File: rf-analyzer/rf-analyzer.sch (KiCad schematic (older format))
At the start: 56 parts, among them U1 AD8302, U2 AD8302, U3 OPA695

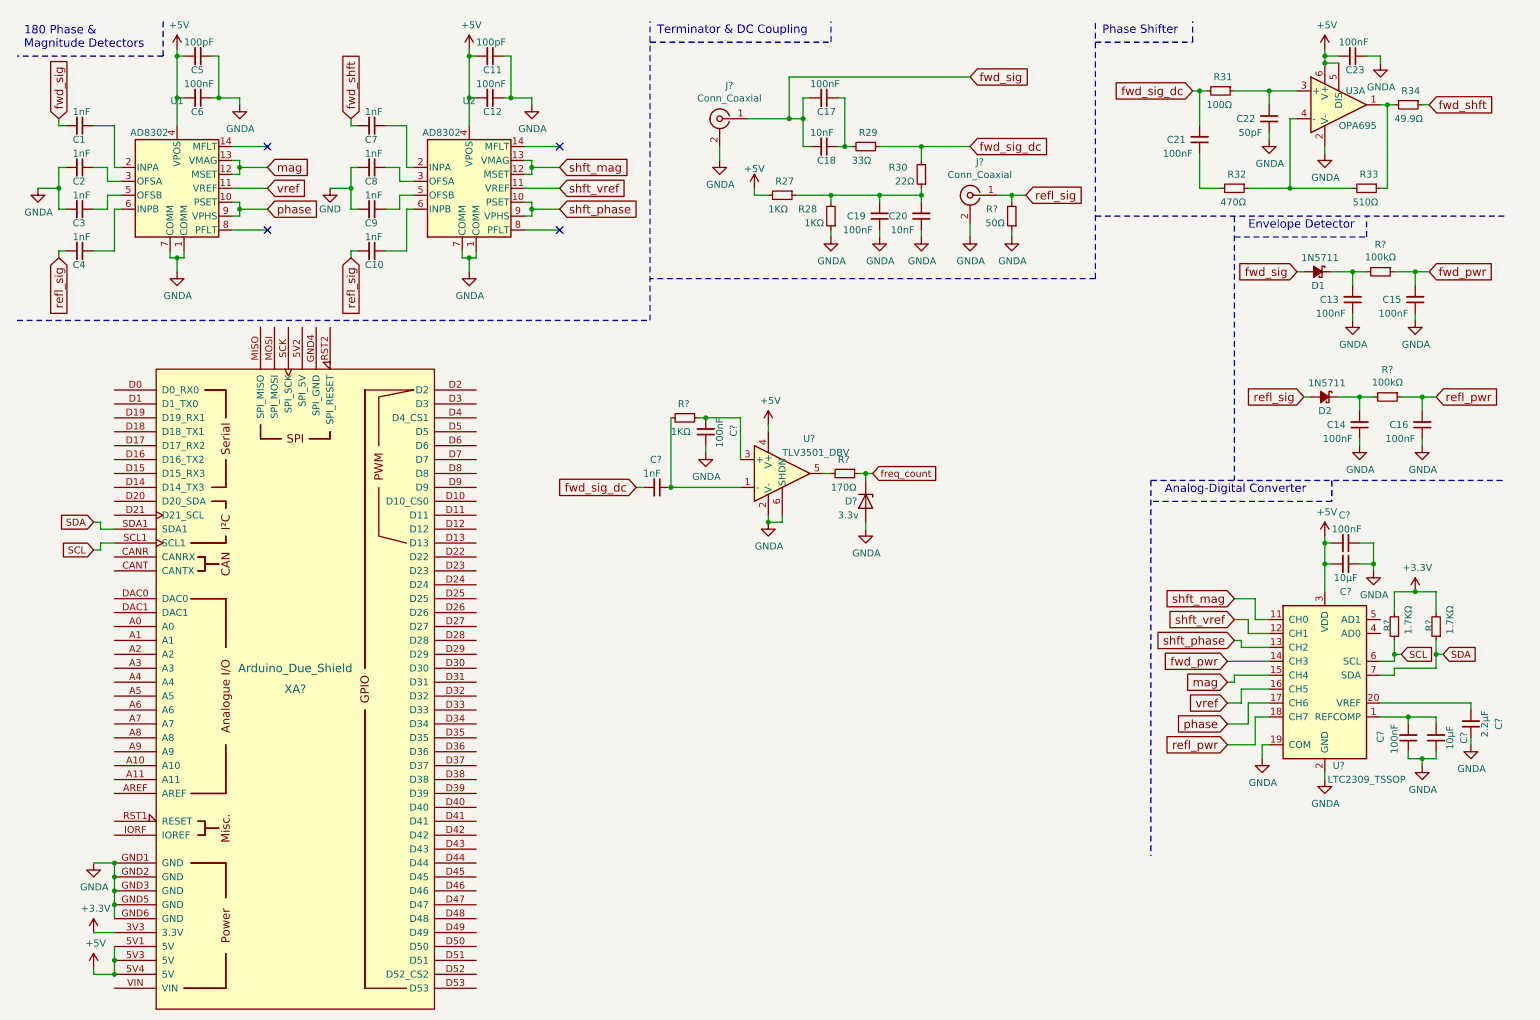
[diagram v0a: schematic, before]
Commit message: Added frequency counter prescaler.
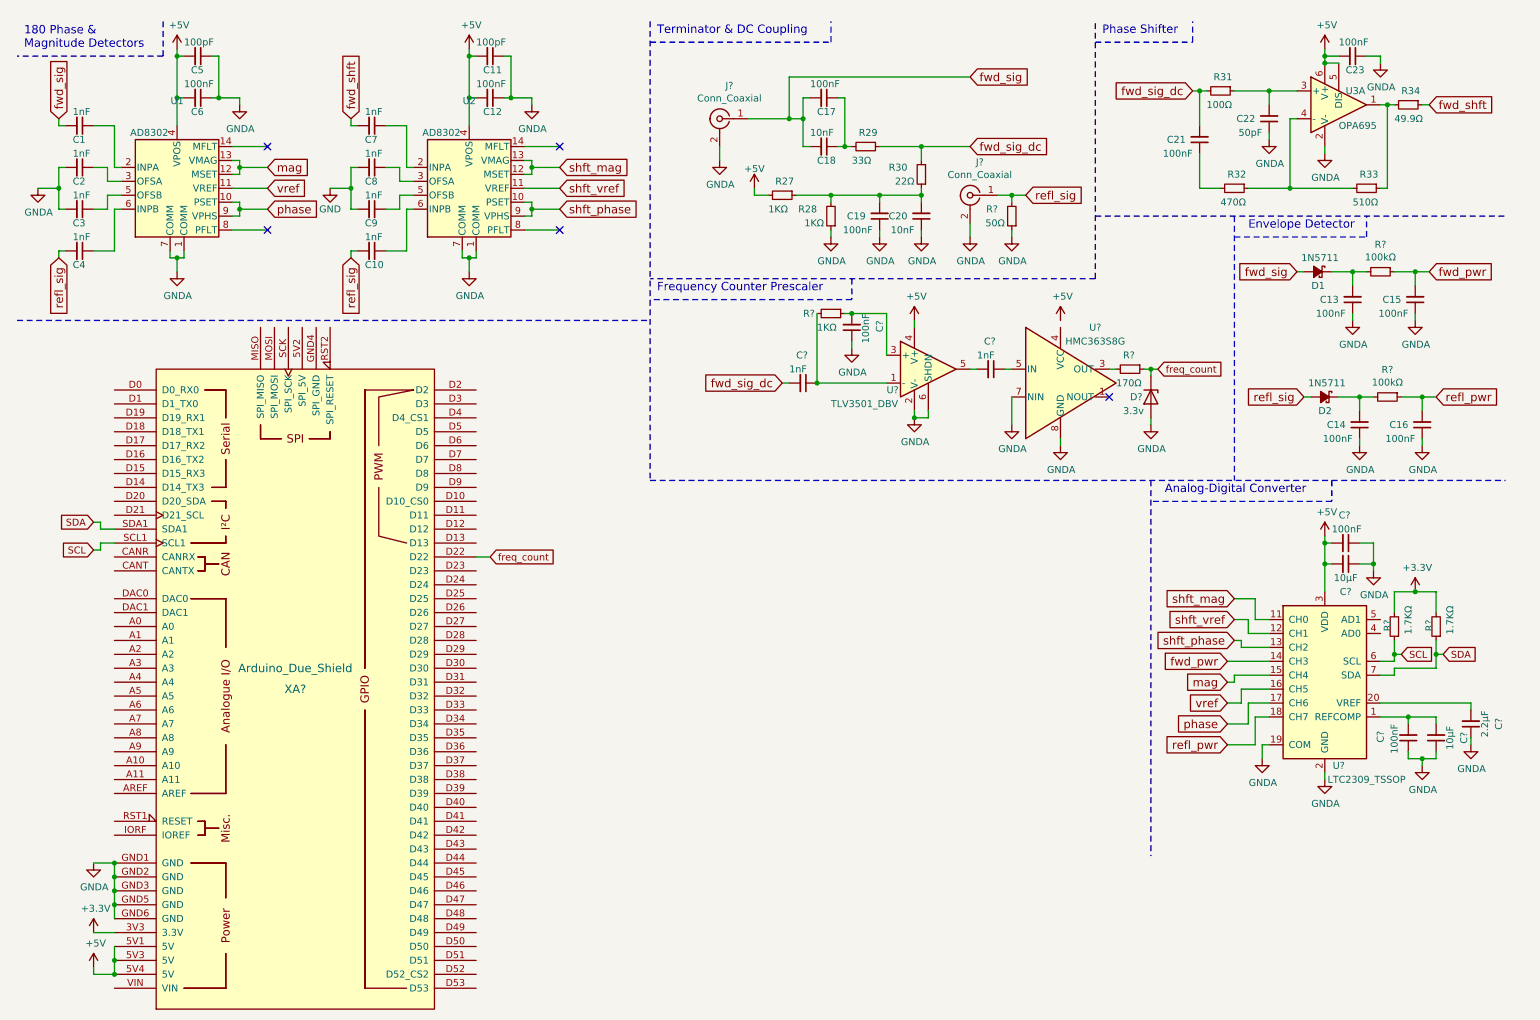
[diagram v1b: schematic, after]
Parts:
- added C?: 1nF, Capacitor_SMD:C_0603_1608Metric_Pad1.05x0.95mm_HandSolder, symbol Device:C_Small
- added U?: HMC363S8G, Package_SO:SOIC-8_3.9x4.9mm_P1.27mm, symbol RF_Freemo:HMC363S8G
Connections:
- net GNDA: now also U?.7 (NIN), U?.8 (GND)
- net freq_count: now also XA?.D22
- net at R?.2: now also U?.3 (OUT); no longer U?.5
- new net: C?.1, U?.5 (IN)
- new net: C?.2, U?.5
- no-connect marks 4 -> 5
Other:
- note added: "Frequency Counter Prescaler"
- moved on the sheet: C?, D?, R?, U?

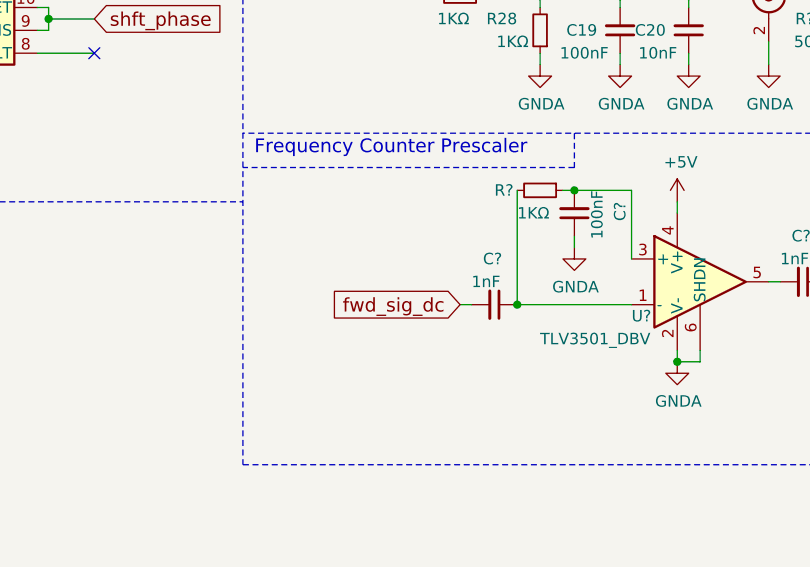
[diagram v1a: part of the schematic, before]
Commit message: Removed decoupling capacitor from prescaler.
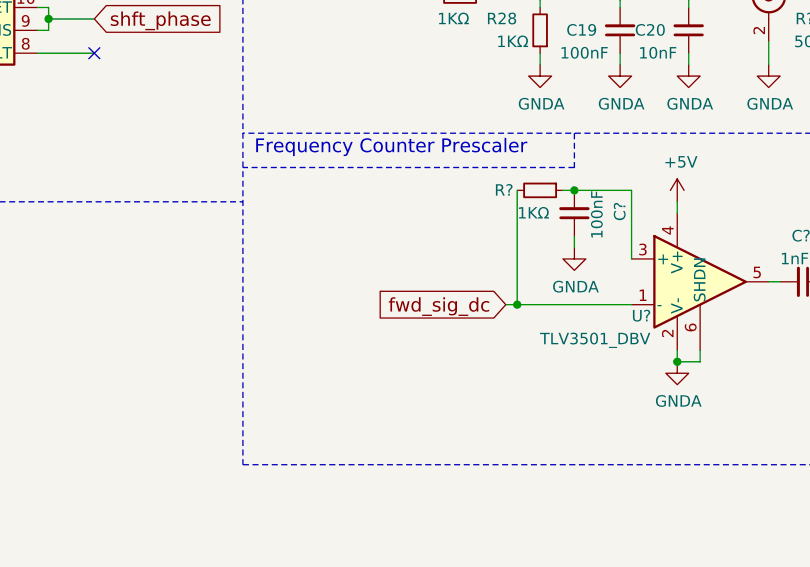
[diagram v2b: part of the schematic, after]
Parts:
- removed C?: 1nF, Capacitor_SMD:C_0603_1608Metric_Pad1.05x0.95mm_HandSolder, symbol Device:C_Small
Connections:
- net fwd_sig_dc: now also R?.2, U?.1 (-)
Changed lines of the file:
@@
 Connection ~ 9900 800
-$Comp
-L Device:C_Small C?
-U 1 1 604F0B98
-P 6150 3100
-F 0 "C?" V 5950 3050 50  0000 L CNN
-F 1 "1nF" V 6050 3000 50  0000 L CNN
-F 2 "Capacitor_SMD:C_0603_1608Metric_Pad1.05x0.95mm_HandSolder" H 6150 3100 50  0001 C CNN
-F 3 "" H 6150 3100 50  0001 C CNN
-	1    6150 3100
-	0    1    1    0
-$EndComp
 $Comp
 L power:GNDA #PWR?
@@
 Wire Wire Line
 	6250 3100 6750 3100
-Connection ~ 6250 3100
 $Comp
 L power:GNDA #PWR?
@@
 	7050 3350 6950 3350
 Connection ~ 6950 3350
-Text GLabel 6000 3100 0    60   Input ~ 0
+Text GLabel 6200 3100 0    60   Input ~ 0
 fwd_sig_dc
 Wire Wire Line
-	6000 3100 6050 3100
+	6200 3100 6250 3100
 $Comp
 L Device:R_Small R?
@@
 	1    0    0    -1
 $EndComp
+Connection ~ 6250 3100
 $EndSCHEMATC

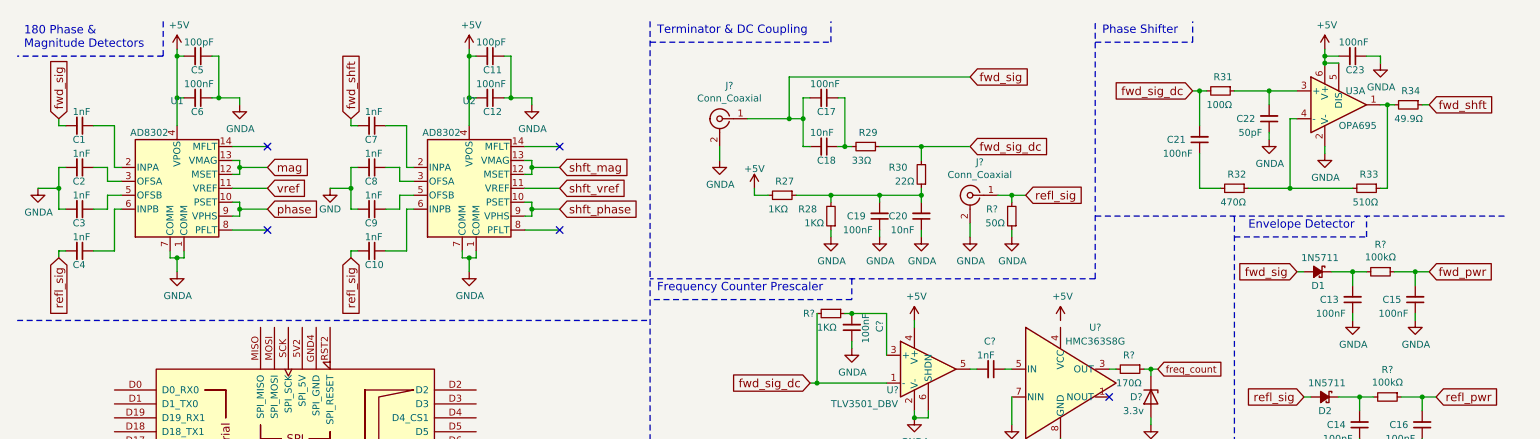
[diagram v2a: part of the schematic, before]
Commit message: Added the decoupling caps in a central location allowing me to reduce the overall number of capacitors.
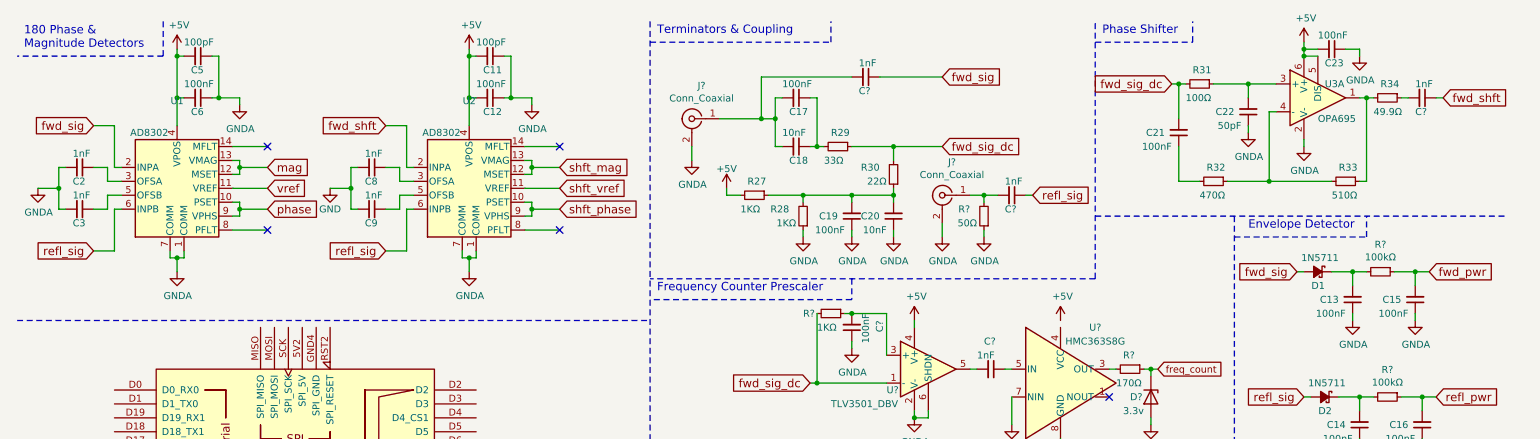
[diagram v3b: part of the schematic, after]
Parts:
- removed C1, C10, C4, C7: 1nF, Capacitor_SMD:C_0603_1608Metric_Pad1.05x0.95mm_HandSolder, symbol Device:C_Small
- added C? (x3): 1nF, Capacitor_SMD:C_0603_1608Metric_Pad1.05x0.95mm_HandSolder, symbol Device:C_Small
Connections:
- net fwd_shft: now also U2.2 (INPA), C?.1; no longer R34.1
- net fwd_sig: now also U1.2 (INPA), C?.1; no longer C17.2, C18.2, J?.1 (In)
- net refl_sig: now also U1.6 (INPB), U2.6 (INPB), C?.1; no longer J?.1 (In), R?.2
- new net: C?.2, R34.1
- new net: C17.2, C18.2, C?.2, J?.1 (In)
- new net: C?.2, J?.1 (In), R?.2
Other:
- note added: "Terminators & Coupling"
- note removed: "Terminator & DC Coupling"
- moved on the sheet: C17, C18, C19, C20, C21, C22, C23, J?, R27, R28, R29, R30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

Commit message: Added shielding to schematic.
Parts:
- added J?: RF_Shield_Two_Pieces, RF_Shielding:Laird_Technologies_BMI-S-230-F_50.8x38.1mm, symbol Device:RF_Shield_Two_Pieces
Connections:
- net GNDA: now also J?.1 (Shield)
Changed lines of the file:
@@
 Wire Wire Line
 	10750 1050 10700 1050
+$Comp
+L Device:RF_Shield_Two_Pieces J?
+U 1 1 5FB2E8F5
+P 5750 4800
+F 0 "J?" H 6480 4864 50  0000 L CNN
+F 1 "RF_Shield_Two_Pieces" H 6480 4773 50  0000 L CNN
+F 2 "RF_Shielding:Laird_Technologies_BMI-S-230-F_50.8x38.1mm" H 5750 4700 50  0001 C CNN
+F 3 "~" H 5750 4700 50  0001 C CNN
+	1    5750 4800
+	1    0    0    -1
+$EndComp
+$Comp
+L power:GNDA #PWR?
+U 1 1 5FB3AD55
+P 5750 5250
+F 0 "#PWR?" H 5750 5000 50  0001 C CNN
+F 1 "GNDA" H 5755 5077 50  0000 C CNN
+F 2 "" H 5750 5250 50  0001 C CNN
+F 3 "" H 5750 5250 50  0001 C CNN
+	1    5750 5250
+	1    0    0    -1
+$EndComp
+Wire Wire Line
+	5750 5200 5750 5250
 $EndSCHEMATC

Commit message: Added a missing wire to a power rail.
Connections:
- net +5V: now also U?.4 (VCC)
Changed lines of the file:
@@
 Wire Wire Line
 	5750 5200 5750 5250
+Wire Wire Line
+	8000 2650 8000 2700
 $EndSCHEMATC

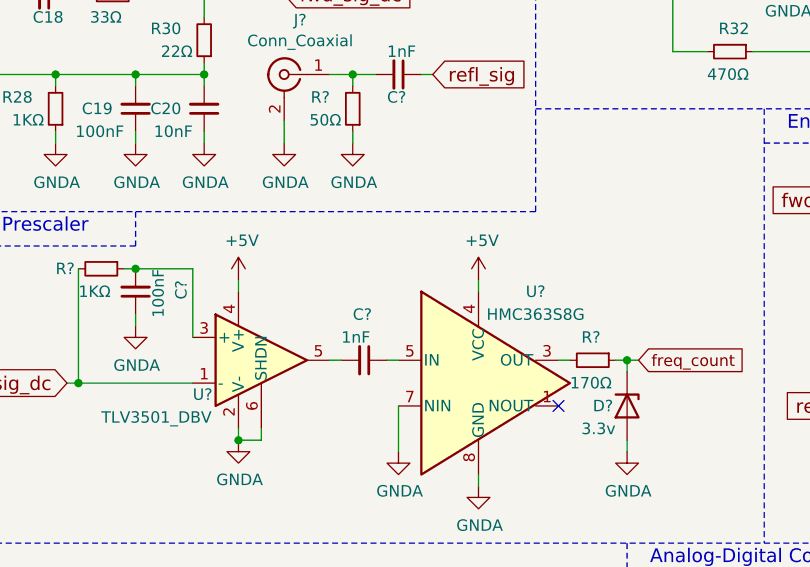
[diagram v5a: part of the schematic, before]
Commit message: Added some missing bypass capacitors.
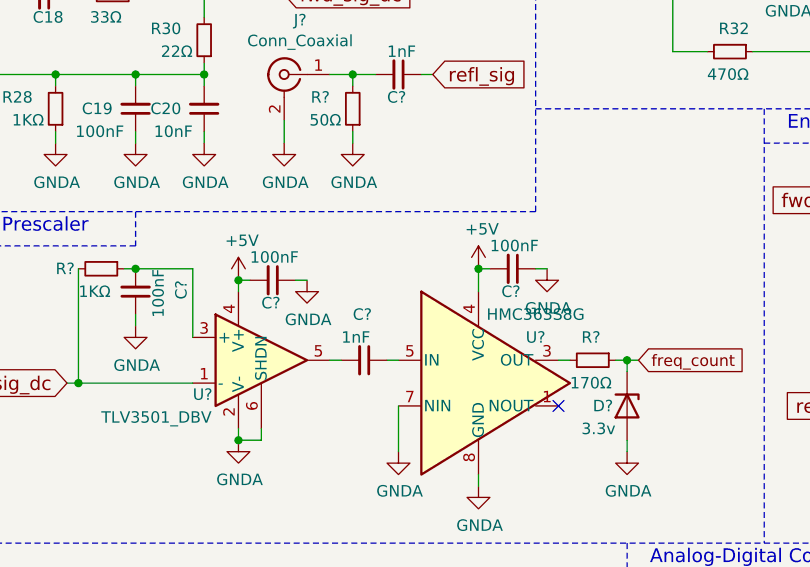
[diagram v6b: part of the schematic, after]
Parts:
- added C? (x2): 100nF, Capacitor_SMD:C_0603_1608Metric_Pad1.05x0.95mm_HandSolder, symbol Device:C_Small
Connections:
- net +5V: now also C?.2, C?.2
- net GNDA: now also C?.1, C?.1
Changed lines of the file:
@@
 U 1 1 5F4F3D4D
 P 8000 3100
-F 0 "U?" H 8250 3500 50  0000 C CNN
+F 0 "U?" H 8250 3300 50  0000 C CNN
 F 1 "HMC363S8G" H 8250 3400 50  0000 C CNN
 F 2 "Package_SO:SOIC-8_3.9x4.9mm_P1.27mm" H 8850 2800 50  0001 C CNN
@@
 L power:+5V #PWR?
 U 1 1 5F5D503E
-P 8000 2650
-F 0 "#PWR?" H 8000 2500 50  0001 C CNN
-F 1 "+5V" H 8015 2823 50  0000 C CNN
-F 2 "" H 8000 2650 50  0001 C CNN
-F 3 "" H 8000 2650 50  0001 C CNN
-	1    8000 2650
+P 8000 2600
+F 0 "#PWR?" H 8000 2450 50  0001 C CNN
+F 1 "+5V" H 8015 2773 50  0000 C CNN
+F 2 "" H 8000 2600 50  0001 C CNN
+F 3 "" H 8000 2600 50  0001 C CNN
+	1    8000 2600
 	1    0    0    -1
 $EndComp
@@
 Wire Wire Line
 	5750 5200 5750 5250
-Wire Wire Line
-	8000 2650 8000 2700
+$Comp
+L Device:C_Small C?
+U 1 1 5FBF94A5
+P 7100 2650
+F 0 "C?" V 7200 2600 50  0000 L CNN
+F 1 "100nF" V 7000 2550 50  0000 L CNN
+F 2 "Capacitor_SMD:C_0603_1608Metric_Pad1.05x0.95mm_HandSolder" H 7100 2650 50  0001 C CNN
+F 3 "" H 7100 2650 50  0001 C CNN
+	1    7100 2650
+	0    1    1    0
+$EndComp
+$Comp
+L Device:C_Small C?
+U 1 1 5FC0DF4B
+P 8150 2600
+F 0 "C?" V 8250 2550 50  0000 L CNN
+F 1 "100nF" V 8050 2500 50  0000 L CNN
+F 2 "Capacitor_SMD:C_0603_1608Metric_Pad1.05x0.95mm_HandSolder" H 8150 2600 50  0001 C CNN
+F 3 "" H 8150 2600 50  0001 C CNN
+	1    8150 2600
+	0    1    1    0
+$EndComp
+$Comp
+L power:GNDA #PWR?
+U 1 1 5FCC9597
+P 7250 2650
+F 0 "#PWR?" H 7250 2400 50  0001 C CNN
+F 1 "GNDA" H 7255 2477 50  0000 C CNN
+F 2 "" H 7250 2650 50  0001 C CNN
+F 3 "" H 7250 2650 50  0001 C CNN
+	1    7250 2650
+	1    0    0    -1
+$EndComp
+$Comp
+L power:GNDA #PWR?
+U 1 1 5FCDCA55
+P 8300 2600
+F 0 "#PWR?" H 8300 2350 50  0001 C CNN
+F 1 "GNDA" H 8305 2427 50  0000 C CNN
+F 2 "" H 8300 2600 50  0001 C CNN
+F 3 "" H 8300 2600 50  0001 C CNN
+	1    8300 2600
+	1    0    0    -1
+$EndComp
+Wire Wire Line
+	7000 2650 6950 2650
+Connection ~ 6950 2650
+Wire Wire Line
+	7200 2650 7250 2650
+Wire Wire Line
+	8250 2600 8300 2600
+Wire Wire Line
+	8050 2600 8000 2600
+Wire Wire Line
+	8000 2600 8000 2700
+Connection ~ 8000 2600
 $EndSCHEMATC
